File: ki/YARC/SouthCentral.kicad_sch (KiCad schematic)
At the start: 0 parts

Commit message: Ongoing development
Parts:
- added U? (x5): 74HC00, symbol 74xx:74HC00
- added U? (x3): 74LS139, symbol 74xx:74LS139
- added U? (x5): 74LS157, symbol 74xx:74LS157
- added U?: 74LS138, symbol 74xx:74LS138
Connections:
- new net: U?.3, U?.3 (I1a)
- new net: U?.11 (O1), U?.6 (I1b)
- new net: U?.12 (O0), U?.6 (I1b)
- new net: U?.13 (I1d), U?.9 (O3)
- new net: U?.1 (S), U?.1 (S), U?.15 (O0)
- new net ALU_NO_OP: U?.7 (O3)
- new net ALU_OP_0: U?.4 (Za)
- new net ALU_OP_1: U?.7 (Zb)
- new net ALU_OP_2: U?.9 (Zc)
- new net ALU_OP_3: U?.12 (Zd)
- new net ALU_PHI_1: U?.4 (O0)
- new net ALU_PHI_2: U?.5 (O1)
- new net GND: U?.1 (E), U?.10 (I1c), U?.10 (I1c), U?.11 (I0c), U?.13 (I1d), U?.14 (I0d), U?.15 (E), U?.15 (E), U?.15 (E), U?.15 (E), U?.15 (E), U?.15 (E), U?.2 (I0a), U?.4 (E1), U?.5 (E2), U?.5 (I0b), U?.5 (I0b), U?.7 (GND), U?.8 (GND), U?.8 (GND), U?.8 (GND), U?.8 (GND), U?.8 (GND), U?.8 (GND), U?.8 (GND)
- new net IRH0: U?.2 (I0a)
- new net IRH1: U?.5 (I0b)
- new net IRH2: U?.11 (I0c)
- new net IRH3: U?.14 (I0d)
- new net IRL0: U?.2 (I0a)
- new net IRL1: U?.5 (I0b)
- new net IRL2: U?.11 (I0c)
- new net IRL3: U?.14 (I0d)
- new net IRL4: U?.2 (I0a)
- new net IRL5: U?.5 (I0b)
- new net IRL6: U?.11 (I0c)
- new net IRL7: U?.14 (I0d)
- new net K13: U?.1 (A0)
- new net K14: U?.2 (A1)
- new net K15: U?.3 (A2)
- new net K18: U?.2 (A0)
- new net K19: U?.3 (A1)
- new net K20: U?.3 (I1a)
- new net K21: U?.6 (I1b)
- new net K22: U?.10 (I1c)
- new net K23: U?.13 (I1d)
- new net K24: U?.3 (I1a)
- new net K25: U?.6 (I1b)
- new net K26: U?.10 (I1c)
- new net K27: U?.13 (I1d)
- new net K28: U?.3 (I1a)
- new net K29: U?.6 (I1b)
- new net K30: U?.10 (I1c)
- new net K31: U?.13 (I1d)
- new net K4: U?.1 (S), U?.1 (S), U?.1 (S)
- new net RSW0: U?.4 (Za)
- new net RSW1: U?.7 (Zb)
- new net RSW2: U?.9 (Zc)
- new net RSW3: U?.12 (Zd)
- new net RSW4: U?.4 (Za)
- new net RSW5: U?.1, U?.13 (A1), U?.2, U?.7 (Zb)
- new net RSW6: U?.9 (Zc)
- new net RSW7: U?.12 (Zd)
- new net VCC: U?.11 (I0c), U?.14 (I0d), U?.14 (VCC), U?.16 (VCC), U?.16 (VCC), U?.16 (VCC), U?.16 (VCC), U?.16 (VCC), U?.16 (VCC), U?.2 (I0a), U?.6 (E3)
- new net ~{ALU_IN_XCV_EN}: U?.14 (A0), U?.3 (I1a), U?.6 (O2)
- new net ~{CONST_EN}: U?.12 (Zd)
- new net ~{GR_EN}: U?.7 (Zb)
- new net ~{SXT_EN}: U?.4 (Za)
- new net ~{SYSDATA_SRC_IS_F}: U?.12 (O3)
- new net ~{SYSDATA_SRC_IS_IR}: U?.13 (O2)
- new net ~{SYSDATA_SRC_IS_MEM}: U?.11 (O4)
- new net ~{SYSDATA_SRC_IS_SP}: U?.14 (O1)
- new net ~{SYSDATA_XCVR_HI_EN}: U?.7 (Zb)
- new net ~{SYSDATA_XCVR_INBOUND}: U?.9 (Zc)
- new net ~{SYSDATA_XCVR_LOW_EN}: U?.4 (Za)
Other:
- note added: "ALU_CTL"
- note added: "RSW_IR_UC"
- note added: "SYSDATA_SRC"
- note added: "~{SYSDATA_SRC_IS_GR}"

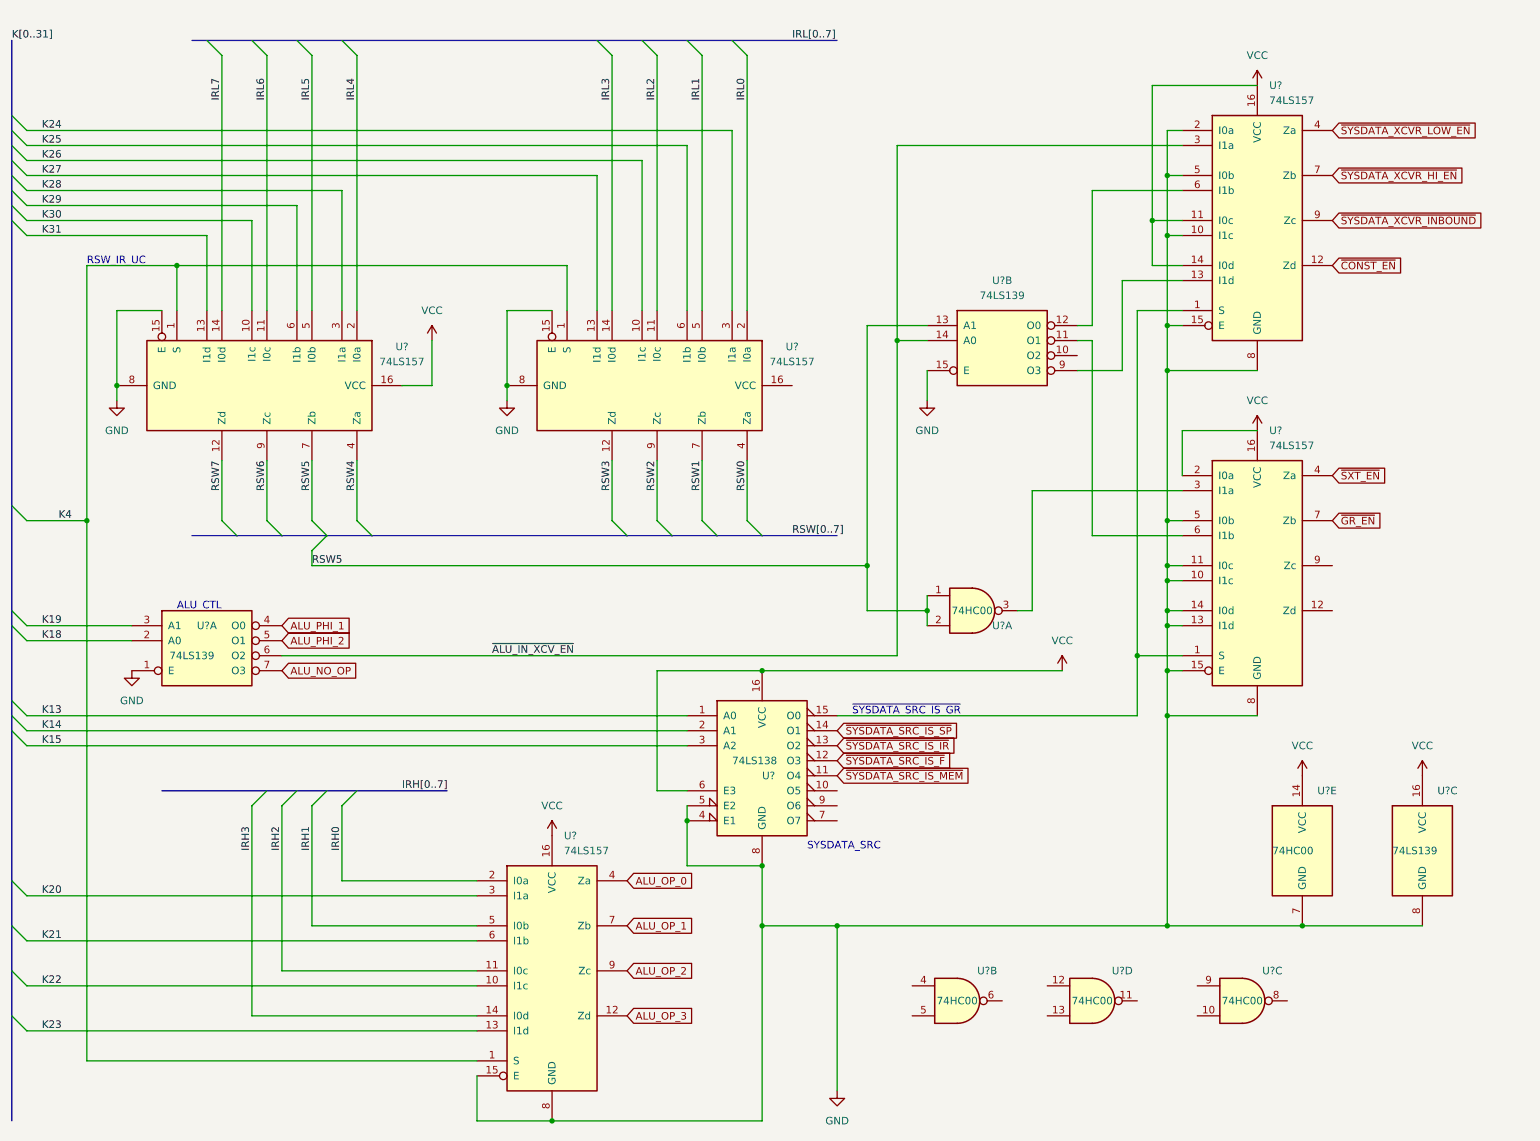
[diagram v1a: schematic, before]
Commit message: Updates to ISA doc. Matching corrections to arch.yasm. Flags layout in Ftz.
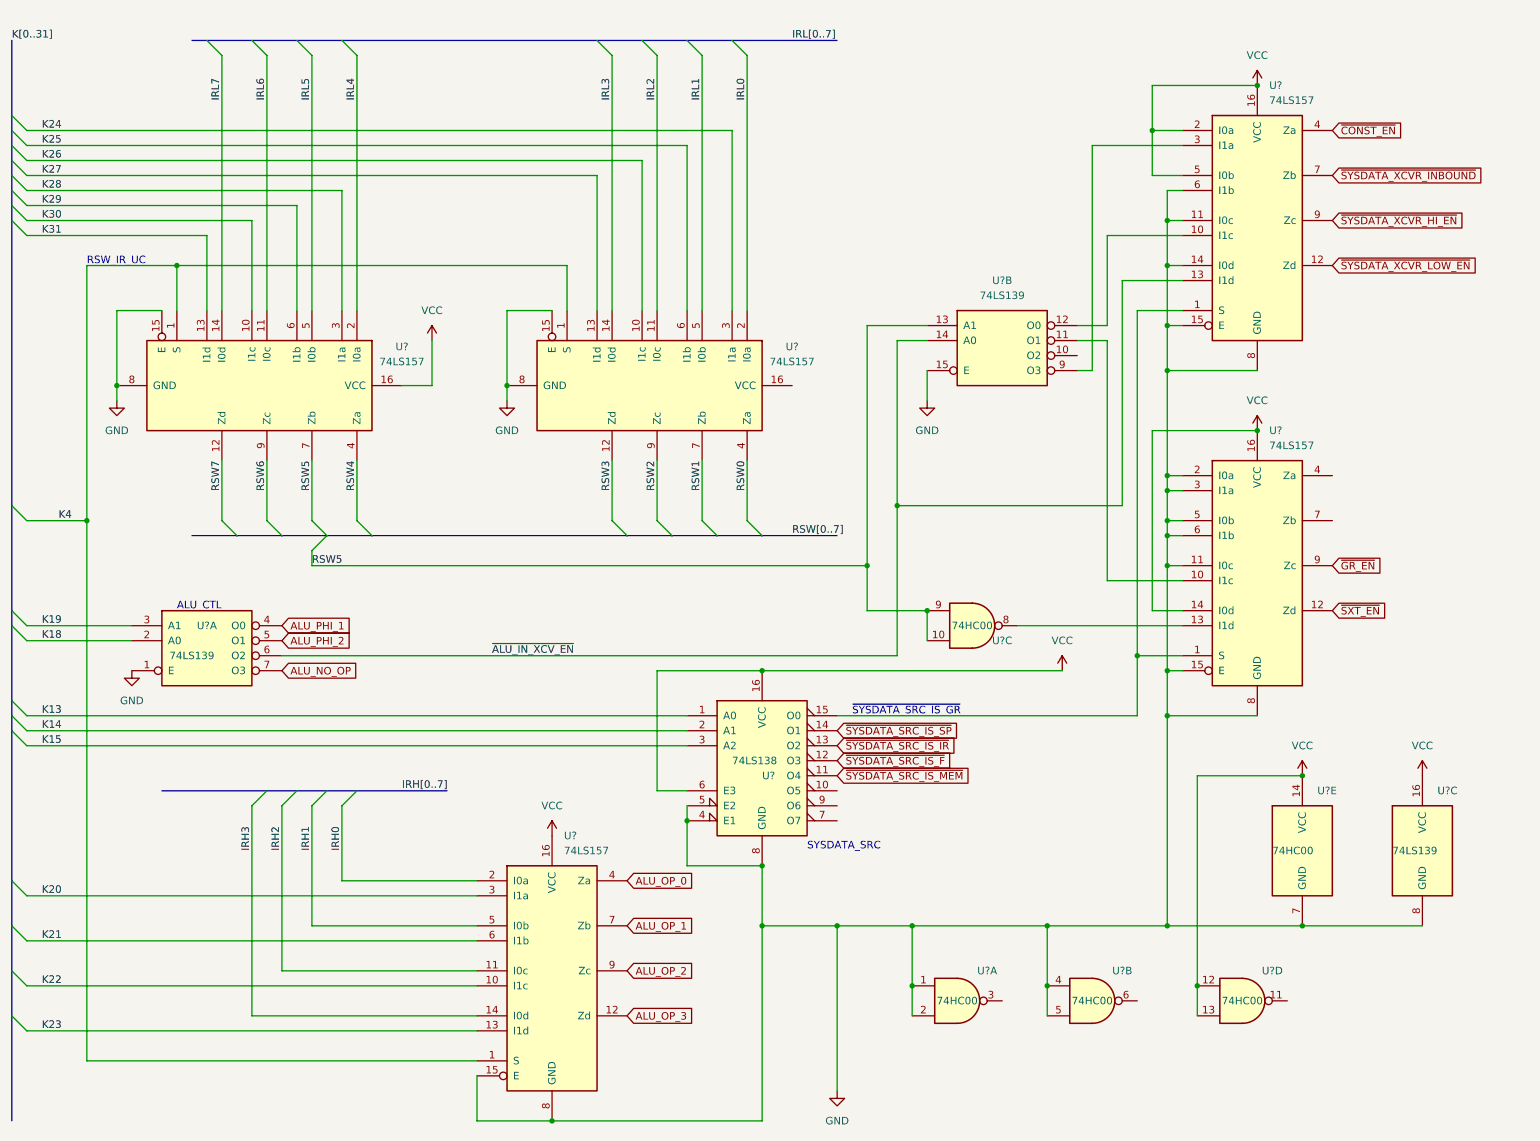
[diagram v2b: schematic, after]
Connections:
- net GND: now also U?.1, U?.11 (I0c), U?.14 (I0d), U?.2, U?.2 (I0a), U?.3 (I1a), U?.4, U?.5, U?.6 (I1b), U?.6 (I1b); no longer U?.10 (I1c), U?.10 (I1c), U?.13 (I1d), U?.14 (I0d), U?.2 (I0a), U?.5 (I0b)
- net RSW5: now also U?.10, U?.9; no longer U?.1, U?.2
- net VCC: now also U?.12, U?.13, U?.14 (I0d), U?.2 (I0a), U?.5 (I0b); no longer U?.11 (I0c), U?.14 (I0d), U?.2 (I0a)
- net ~{ALU_IN_XCV_EN}: now also U?.13 (I1d); no longer U?.3 (I1a)
- net ~{CONST_EN}: now also U?.4 (Za); no longer U?.12 (Zd)
- net ~{GR_EN}: now also U?.9 (Zc); no longer U?.7 (Zb)
- net ~{SXT_EN}: now also U?.12 (Zd); no longer U?.4 (Za)
- net ~{SYSDATA_XCVR_HI_EN}: now also U?.9 (Zc); no longer U?.7 (Zb)
- net ~{SYSDATA_XCVR_INBOUND}: now also U?.7 (Zb); no longer U?.9 (Zc)
- net ~{SYSDATA_XCVR_LOW_EN}: now also U?.12 (Zd); no longer U?.4 (Za)
- net at U?.11 (O1): now also U?.10 (I1c); no longer U?.6 (I1b)
- net at U?.12 (O0): now also U?.10 (I1c); no longer U?.6 (I1b)
- net at U?.9 (O3): now also U?.3 (I1a); no longer U?.13 (I1d)
- new net: U?.13 (I1d), U?.8
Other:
- moved on the sheet: U?C

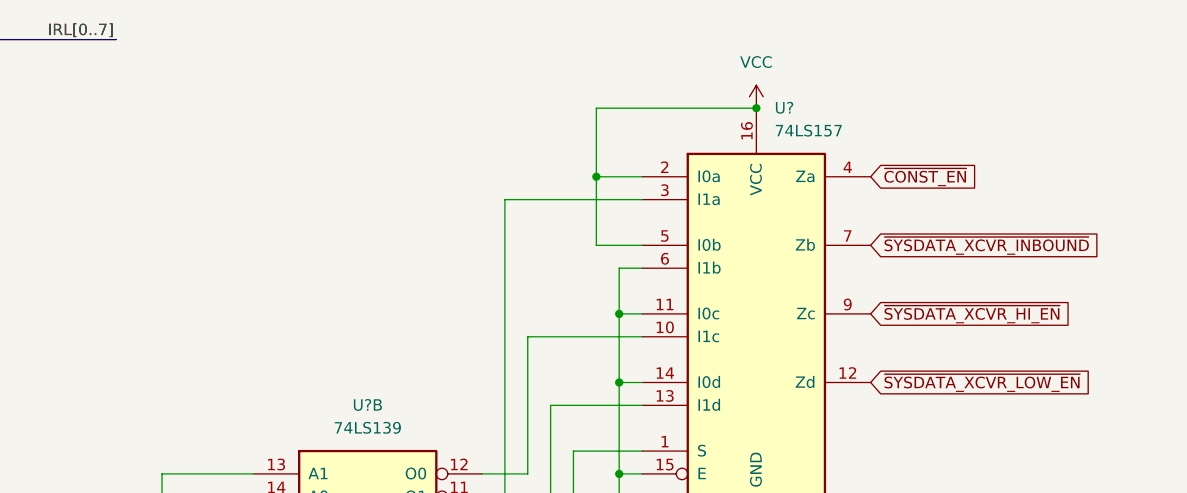
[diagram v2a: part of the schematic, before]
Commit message: Additional wiring updates. Add SetK protocol command and remove much of breakpoint logic from protocol.
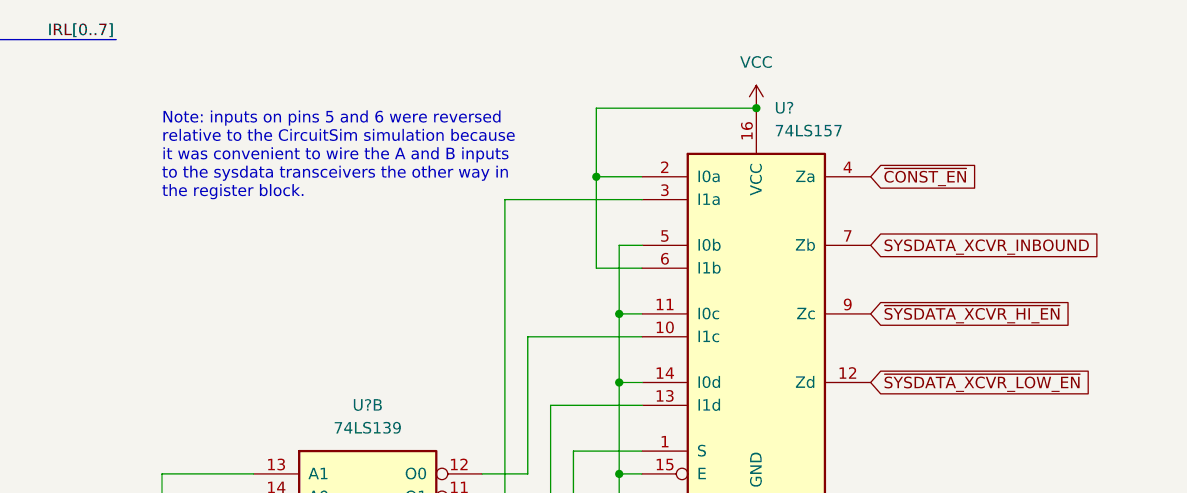
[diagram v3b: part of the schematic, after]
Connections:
- net GND: now also U?.5 (I0b); no longer U?.6 (I1b)
- net VCC: now also U?.6 (I1b); no longer U?.5 (I0b)
- net ~{SYSDATA_XCVR_INBOUND} renamed SYSDATA_XCVR_INBOUND
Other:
- note added: "Note: inputs on pins 5 and 6 were reversed relative to the CircuitSim simulation because it was convenient to wire the A and B inputs to the sysdata transceivers the other way in the register block."
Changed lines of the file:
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@@
     (stroke (width 0) (type default) (color 0 0 0 0))
   )
-  (wire (pts (xy 208.28 33.02) (xy 208.28 40.64))
+  (wire (pts (xy 208.28 33.02) (xy 208.28 43.18))
     (stroke (width 0) (type default) (color 0 0 0 0))
   )
@@
     (stroke (width 0) (type default) (color 0 0 0 0))
   )
-  (wire (pts (xy 213.36 43.18) (xy 210.82 43.18))
-    (stroke (width 0) (type default) (color 0 0 0 0))
-  )
   (wire (pts (xy 160.02 66.04) (xy 160.02 106.68))
     (stroke (width 0) (type default) (color 0 0 0 0))
@@
     (stroke (width 0) (type default) (color 0 0 0 0))
   )
-  (wire (pts (xy 210.82 43.18) (xy 210.82 48.26))
+  (wire (pts (xy 210.82 40.64) (xy 210.82 48.26))
     (stroke (width 0) (type default) (color 0 0 0 0))
   )
@@
     (stroke (width 0) (type default) (color 0 0 0 0))
   )
+  (wire (pts (xy 208.28 43.18) (xy 213.36 43.18))
+    (stroke (width 0) (type default) (color 0 0 0 0))
+  )
   (bus (pts (xy 15.24 134.62) (xy 15.24 160.02))
     (stroke (width 0) (type default) (color 0 0 0 0))
@@
     (stroke (width 0) (type default) (color 0 0 0 0))
   )
+  (wire (pts (xy 213.36 40.64) (xy 210.82 40.64))
+    (stroke (width 0) (type default) (color 0 0 0 0))
+  )
   (wire (pts (xy 213.36 91.44) (xy 210.82 91.44))
     (stroke (width 0) (type default) (color 0 0 0 0))
@@
     (stroke (width 0) (type default) (color 0 0 0 0))
   )
-  (wire (pts (xy 213.36 40.64) (xy 208.28 40.64))
-    (stroke (width 0) (type default) (color 0 0 0 0))
-  )
   (wire (pts (xy 73.66 99.06) (xy 73.66 88.9))
     (stroke (width 0) (type default) (color 0 0 0 0))
@@
     (effects (font (size 1.27 1.27)) (justify left bottom))
   )
+  (text "Note: inputs on pins 5 and 6 were reversed\nrelative to the CircuitSim simulation because\nit was convenient to wire the A and B inputs\nto the sysdata transceivers the other way in\nthe register block."
+    (at 160.02 35.56 0)
+    (effects (font (size 1.27 1.27)) (justify left bottom))
+  )
   (text "SYSDATA_SRC" (at 149.86 154.94 0)
     (effects (font (size 1.27 1.27)) (justify left bottom))
@@
     )
   )
-  (global_label "~{SYSDATA_XCVR_INBOUND}" (shape input) (at 238.76 40.64 0) (fields_autoplaced)
+  (global_label "SYSDATA_XCVR_INBOUND" (shape input) (at 238.76 40.64 0) (fields_autoplaced)
     (effects (font (size 1.27 1.27)) (justify left))
     (property "Intersheet References" "${INTERSHEET_REFS}" (id 0) (at 264.3355 40.5606 0)
